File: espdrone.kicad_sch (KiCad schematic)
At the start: 60 parts, among them J6 Conn_01x06, U2 USBLC6-2P6, U3 W25Q128JVP, Y1 Crystal_GND24

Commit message: Route some peripherals
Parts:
- removed C6: 100n, Capacitor_SMD:C_0402_1005Metric, symbol Device:C
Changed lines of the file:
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@@
 	)
 	(junction
-		(at 55.88 223.52)
-		(diameter 0)
-		(color 0 0 0 0)
-	)
-	(junction
 		(at 109.22 264.16)
 		(diameter 0)
@@
 	)
 	(junction
-		(at 44.45 233.68)
-		(diameter 0)
-		(color 0 0 0 0)
-	)
-	(junction
 		(at 232.41 220.98)
 		(diameter 0)
@@
 	(wire
 		(pts
-			(xy 44.45 232.41) (xy 44.45 233.68)
+			(xy 44.45 232.41) (xy 44.45 234.95)
 		)
 		(stroke
@@
 	(wire
 		(pts
-			(xy 55.88 233.68) (xy 44.45 233.68)
-		)
-		(stroke
-			(width 0)
-			(type default)
-		)
-	)
-	(wire
-		(pts
 			(xy 255.27 231.14) (xy 255.27 232.41)
 		)
@@
 	(wire
 		(pts
-			(xy 55.88 232.41) (xy 55.88 233.68)
-		)
-		(stroke
-			(width 0)
-			(type default)
-		)
-	)
-	(wire
-		(pts
 			(xy 285.75 142.24) (xy 285.75 151.13)
 		)
@@
 	(wire
 		(pts
-			(xy 44.45 233.68) (xy 44.45 234.95)
-		)
-		(stroke
-			(width 0)
-			(type default)
-		)
-	)
-	(wire
-		(pts
 			(xy 217.17 166.37) (xy 218.44 166.37)
 		)
@@
 	(wire
 		(pts
-			(xy 55.88 223.52) (xy 55.88 224.79)
-		)
-		(stroke
-			(width 0)
-			(type default)
-		)
-	)
-	(wire
-		(pts
-			(xy 55.88 223.52) (xy 44.45 223.52)
-		)
-		(stroke
-			(width 0)
-			(type default)
-		)
-	)
-	(wire
-		(pts
 			(xy 87.63 73.66) (xy 87.63 74.93)
 		)
@@
 	(wire
 		(pts
-			(xy 55.88 223.52) (xy 106.68 223.52)
+			(xy 44.45 223.52) (xy 106.68 223.52)
 		)
 		(stroke
@@
 					(unit 1)
 				)
-			)
-		)
-	)
-	(symbol
-		(lib_id "Device:C")
-		(at 55.88 228.6 0)
-		(mirror y)
-		(unit 1)
-		(body_style 1)
-		(exclude_from_sim no)
-		(in_bom yes)
-		(on_board yes)
-		(in_pos_files yes)
-		(dnp no)
-		(property "Reference" "C6"
-			(at 52.832 227.33 0)
-			(show_name no)
-			(do_not_autoplace no)
-			(effects
-				(font
-					(size 1.27 1.27)
-				)
-				(justify left)
-			)
-		)
-		(property "Value" "100n"
-			(at 53.086 229.87 0)
-			(show_name no)
-			(do_not_autoplace no)
-			(effects
-				(font
-					(size 1.27 1.27)
-				)
-				(justify left)
-			)
-		)
-		(property "Footprint" "Capacitor_SMD:C_0402_1005Metric"
-			(at 54.9148 232.41 0)
-			(hide yes)
-			(show_name no)
-			(do_not_autoplace no)
-			(effects
-				(font
-					(size 1.27 1.27)
-				)
-			)
-		)
-		(property "Datasheet" ""
-			(at 55.88 228.6 0)
-			(hide yes)
-			(show_name no)
-			(do_not_autoplace no)
-			(effects
-				(font
-					(size 1.27 1.27)
-				)
-			)
-		)
-		(property "Description" "Unpolarized capacitor"
-			(at 55.88 228.6 0)
-			(hide yes)
-			(show_name no)
-			(do_not_autoplace no)
-			(effects
-				(font
-					(size 1.27 1.27)
-				)
-			)
-		)
-		(pin "1"
-		)
-		(pin "2"
-		)
-		(instances
-			(project "espdrone"
-				(path "/6e047eb1-70b3-49d8-916c-92a2df32e839"
-					(reference "C6")
-					(unit 1)
-				)

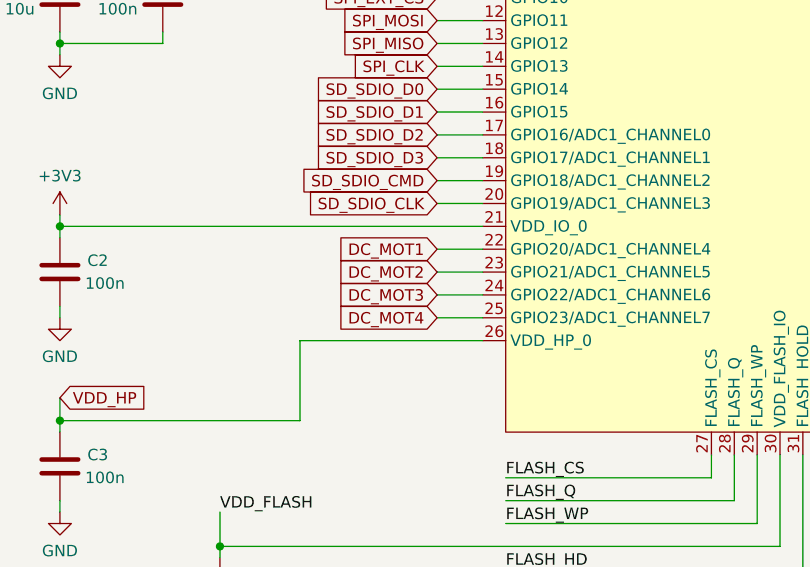
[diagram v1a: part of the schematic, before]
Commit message: Remove brushed motor control and WS2812B LEDs
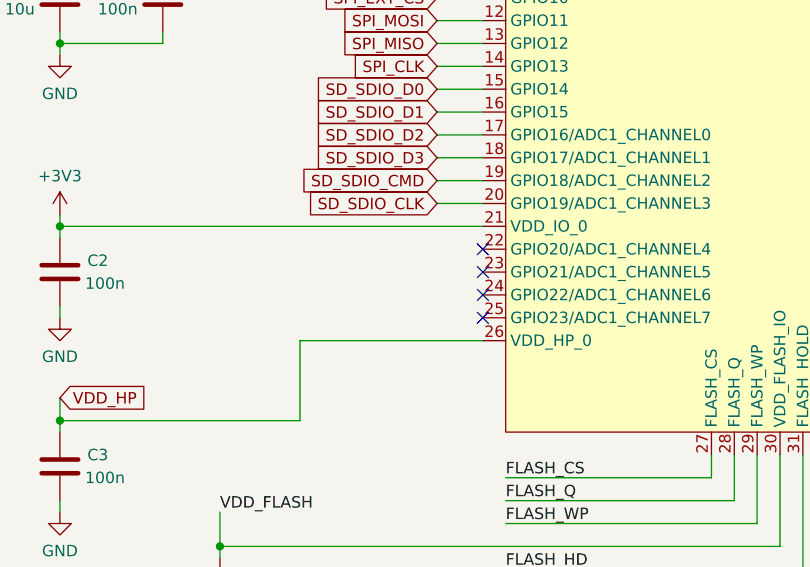
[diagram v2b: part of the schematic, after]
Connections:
- net DC_MOT1: no longer names the net of U1.22 (GPIO20/ADC1_CHANNEL4)
- net DC_MOT2: no longer names the net of U1.23 (GPIO21/ADC1_CHANNEL5)
- net DC_MOT3: no longer names the net of U1.24 (GPIO22/ADC1_CHANNEL6)
- net DC_MOT4: no longer names the net of U1.25 (GPIO23/ADC1_CHANNEL7)
- no-connect marks 27 -> 31
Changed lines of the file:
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@@
 	)
 	(no_connect
+		(at 73.66 190.5)
+	)
+	(no_connect
 		(at 157.48 213.36)
 	)
@@
 	)
 	(no_connect
+		(at 73.66 198.12)
+	)
+	(no_connect
 		(at 190.5 173.99)
 	)
@@
 	)
 	(no_connect
+		(at 73.66 195.58)
+	)
+	(no_connect
 		(at 132.08 213.36)
 	)
@@
 		(at 73.66 142.24)
 	)
+	(no_connect
+		(at 73.66 193.04)
+	)
 	(wire
 		(pts
@@
 	(wire
 		(pts
-			(xy 68.58 195.58) (xy 73.66 195.58)
-		)
-		(stroke
-			(width 0)
-			(type default)
-		)
-	)
-	(wire
-		(pts
 			(xy 147.32 233.68) (xy 177.8 233.68)
 		)
@@
 	(wire
 		(pts
-			(xy 68.58 198.12) (xy 73.66 198.12)
-		)
-		(stroke
-			(width 0)
-			(type default)
-		)
-	)
-	(wire
-		(pts
 			(xy 157.48 116.84) (xy 165.1 116.84)
 		)
@@
 	(wire
 		(pts
-			(xy 68.58 193.04) (xy 73.66 193.04)
-		)
-		(stroke
-			(width 0)
-			(type default)
-		)
-	)
-	(wire
-		(pts
 			(xy 287.02 46.99) (xy 287.02 41.91)
 		)
@@
 	(wire
 		(pts
-			(xy 68.58 190.5) (xy 73.66 190.5)
-		)
-		(stroke
-			(width 0)
-			(type default)
-		)
-	)
-	(wire
-		(pts
 			(xy 44.45 223.52) (xy 106.68 223.52)
 		)
@@
 		)
 	)
-	(global_label "DC_MOT3"
-		(shape input)
-		(at 68.58 195.58 180)
-		(fields_autoplaced yes)
-		(effects
-			(font
-				(size 1.27 1.27)
-			)
-			(justify right)
-		)
-		(property "Intersheetrefs" "${INTERSHEET_REFS}"
-			(at 57.1282 195.58 0)
-			(hide yes)
-			(show_name no)
-			(do_not_autoplace no)
-			(effects
-				(font
-					(size 1.27 1.27)
-				)
-				(justify right)
-			)
-		)
-	)
 	(global_label "DSHOT_2"
 		(shape input)
@@
 		)
 	)
-	(global_label "DC_MOT4"
-		(shape input)
-		(at 68.58 198.12 180)
-		(fields_autoplaced yes)
-		(effects
-			(font
-				(size 1.27 1.27)
-			)
-			(justify right)
-		)
-		(property "Intersheetrefs" "${INTERSHEET_REFS}"
-			(at 57.1282 198.12 0)
-			(hide yes)
-			(show_name no)
-			(do_not_autoplace no)
-			(effects
-				(font
-					(size 1.27 1.27)
-				)
-				(justify right)
-			)
-		)
-	)
-	(global_label "DC_MOT2"
-		(shape input)
-		(at 68.58 193.04 180)
-		(fields_autoplaced yes)
-		(effects
-			(font
-				(size 1.27 1.27)
-			)
-			(justify right)
-		)
-		(property "Intersheetrefs" "${INTERSHEET_REFS}"
-			(at 57.1282 193.04 0)
-			(hide yes)
-			(show_name no)
-			(do_not_autoplace no)
-			(effects
-				(font
-					(size 1.27 1.27)
-				)
-				(justify right)
-			)
-		)
-	)
 	(global_label "TELEMETRY"
 		(shape input)
@@
 			)
 		)
-	)
-	(global_label "DC_MOT1"
-		(shape input)
-		(at 68.58 190.5 180)
-		(fields_autoplaced yes)
-		(effects
-			(font
-				(size 1.27 1.27)
-			)
-			(justify right)
-		)
-		(property "Intersheetrefs" "${INTERSHEET_REFS}"
-			(at 57.1282 190.5 0)
-			(hide yes)
-			(show_name no)
-			(do_not_autoplace no)
-			(effects
-				(font
-					(size 1.27 1.27)
-				)
-				(justify right)
-			)
-		)

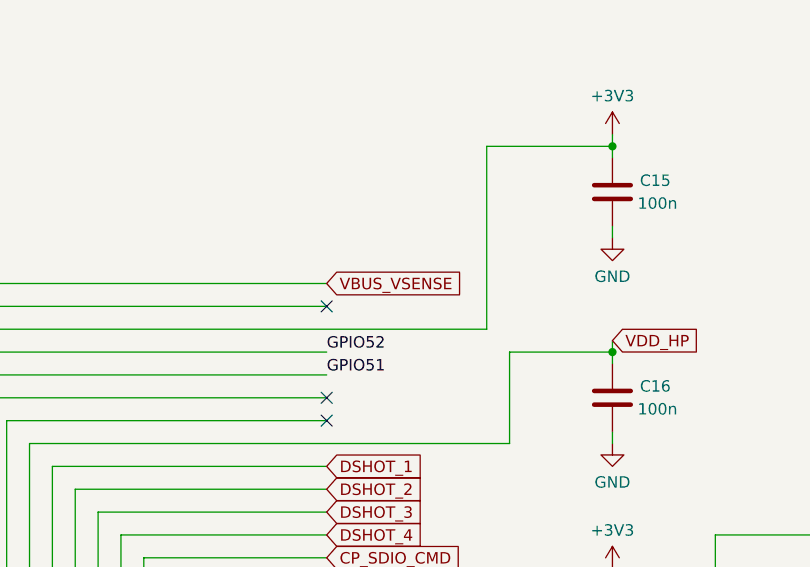
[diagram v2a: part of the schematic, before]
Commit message: Remove external SPI connections and switch voltage measurement from VBUS to +BAT
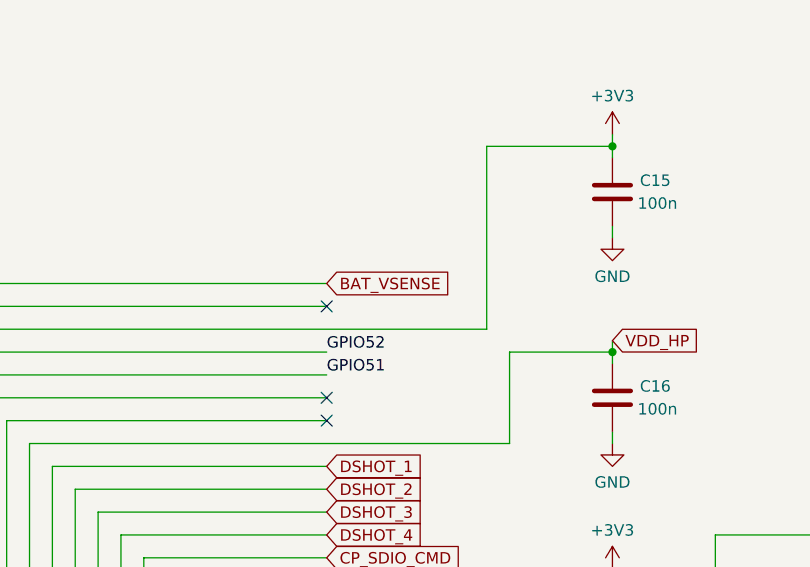
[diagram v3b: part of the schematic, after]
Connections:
- net VBUS_VSENSE renamed BAT_VSENSE
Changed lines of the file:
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@@
 		)
 	)
-	(global_label "VBUS_VSENSE"
+	(global_label "BAT_VSENSE"
 		(shape input)
 		(at 165.1 73.66 0)
@@
 		)
 		(property "Intersheetrefs" "${INTERSHEET_REFS}"
-			(at 181.0875 73.66 0)
+			(at 179.5151 73.66 0)
 			(hide yes)
 			(show_name no)

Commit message: New board cuedge cut
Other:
- company: All-in-one drone flight controller, camera and ESC -> All-in-one drone flight controller, camera and 2S-3S ESC
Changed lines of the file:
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@@
 		(date "2026-08-28")
 		(rev "1.0")
-		(company "All-in-one drone flight controller, camera and ESC")
+		(company "All-in-one drone flight controller, camera and 2S-3S ESC")
 		(comment 1 "ESP32 P4 + ESP32 C5, 4xAM32 ESCs")
-		(comment 2 "1S DC motors, 2S-3S BLDC motors")
 	)
 	(rectangle

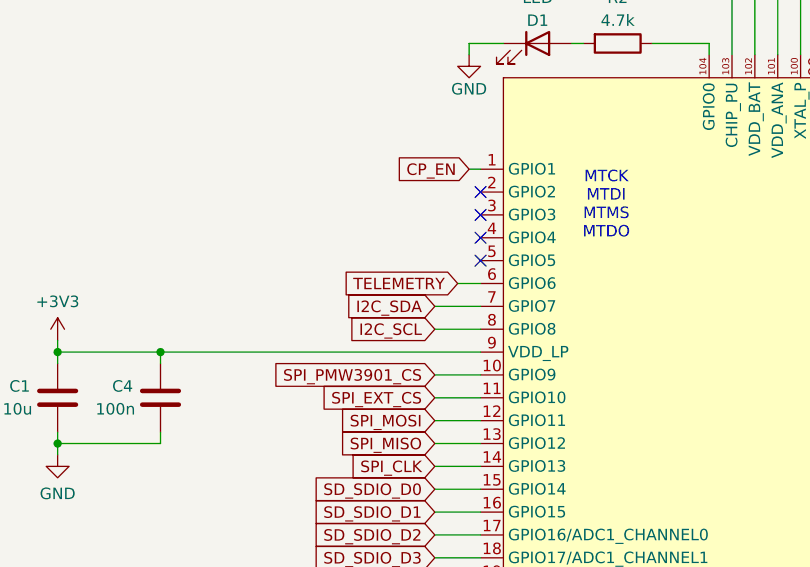
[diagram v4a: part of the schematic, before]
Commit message: Small routing changes
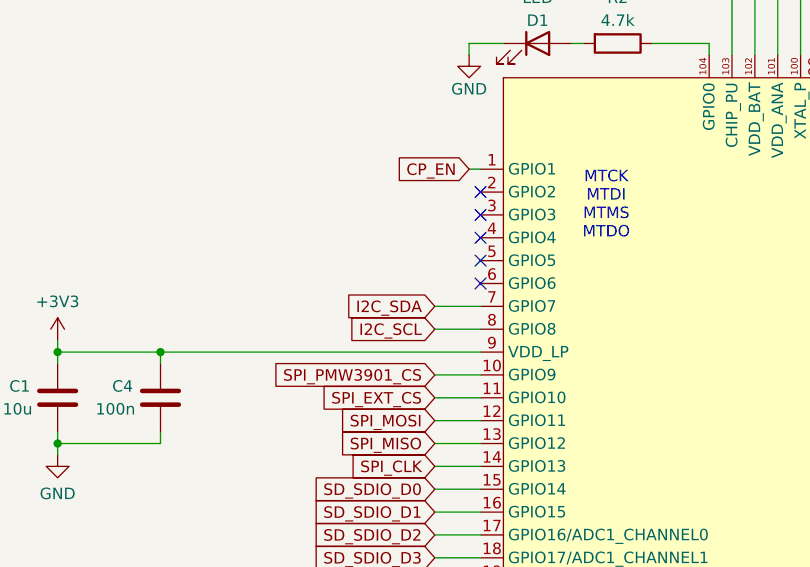
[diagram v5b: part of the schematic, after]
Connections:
- net TELEMETRY: no longer names the net of U1.6 (GPIO6)
- no-connect marks 31 -> 32
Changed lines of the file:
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@@
 	)
 	(no_connect
+		(at 73.66 149.86)
+	)
+	(no_connect
 		(at 190.5 168.91)
 	)
@@
 	(wire
 		(pts
-			(xy 71.12 149.86) (xy 73.66 149.86)
-		)
-		(stroke
-			(width 0)
-			(type default)
-		)
-	)
-	(wire
-		(pts
 			(xy 372.11 71.12) (xy 372.11 72.39)
 		)
@@
 			)
 		)
-	)
-	(global_label "TELEMETRY"
-		(shape input)
-		(at 71.12 149.86 180)
-		(fields_autoplaced yes)
-		(effects
-			(font
-				(size 1.27 1.27)
-			)
-			(justify right)
-		)
-		(property "Intersheetrefs" "${INTERSHEET_REFS}"
-			(at 57.9145 149.86 0)
-			(hide yes)
-			(show_name no)
-			(do_not_autoplace no)
-			(effects
-				(font
-					(size 1.27 1.27)
-				)
-				(justify right)
-			)
-		)

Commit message: Minimize passive footprints again and switch ESC mcu to smaller footprint
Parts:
- removed J6: Conn_01x06, easyeda2kicad:Connector_Pad_1.27mm_1x06, symbol Connector_Generic:Conn_01x06
- removed R8, R9: 10, Resistor_SMD:R_0402_1005Metric, symbol Device:R
- added R49, R51: 10k, Capacitor_SMD:C_0201_0603Metric, symbol Device:R
- C10, C13, C14, C15, C16, C17, C19, C2, C20, C21, C22, C23, C24, C26, C28, C3, C34, C4, C9: footprint Capacitor_SMD:C_0402_1005Metric -> Capacitor_SMD:C_0201_0603Metric
- C29: footprint Capacitor_SMD:C_0603_1608Metric -> Capacitor_SMD:C_0402_1005Metric
- C7: value 100n -> 1u
- R1, R10, R11, R12, R15, R161, R162, R163, R164, R24, R5: footprint Resistor_SMD:R_0402_1005Metric -> Resistor_SMD:R_0201_0603Metric
- R6, R7: footprint Resistor_SMD:R_0402_1005Metric -> Capacitor_SMD:C_0201_0603Metric
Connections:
- net SPI_EXT_CS is gone; now on net SPI_PMW3901_CS: U1.11 (GPIO10)
- net +3V3: now also R49.2, R51.2
- net I2C_SCL: now also R49.1
- net I2C_SDA: now also R51.1
- net SPI_PMW3901_CS: no longer U1.10 (GPIO9)
- net SD_SDIO_CLK: no longer names the net of U1.20 (GPIO19/ADC1_CHANNEL3)
- net SD_SDIO_CMD: no longer names the net of U1.19 (GPIO18/ADC1_CHANNEL2)
- net SD_SDIO_D0: no longer names the net of U1.15 (GPIO14)
- net SD_SDIO_D1: no longer names the net of U1.16 (GPIO15)
- net SD_SDIO_D2: no longer names the net of U1.17 (GPIO16/ADC1_CHANNEL0)
- net SD_SDIO_D3: no longer names the net of U1.18 (GPIO17/ADC1_CHANNEL1)
- no-connect marks 32 -> 39
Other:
- note removed: "UART+GPIO breakout"
- moved on the sheet: C5

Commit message: Apply ESC layout to all 4 ESCs
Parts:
- USB1: footprint easyeda2kicad:USB-C-SMD_TYPE-C-16PIN-2MD-073 -> easyeda2kicad:USB-C-SMD_TYPE-C-16P-USB4110-GF-A
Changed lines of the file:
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@@
 			)
 		)
-		(property "Footprint" "easyeda2kicad:USB-C-SMD_TYPE-C-16PIN-2MD-073"
+		(property "Footprint" "easyeda2kicad:USB-C-SMD_TYPE-C-16P-USB4110-GF-A"
 			(at 275.59 82.55 0)
 			(hide yes)

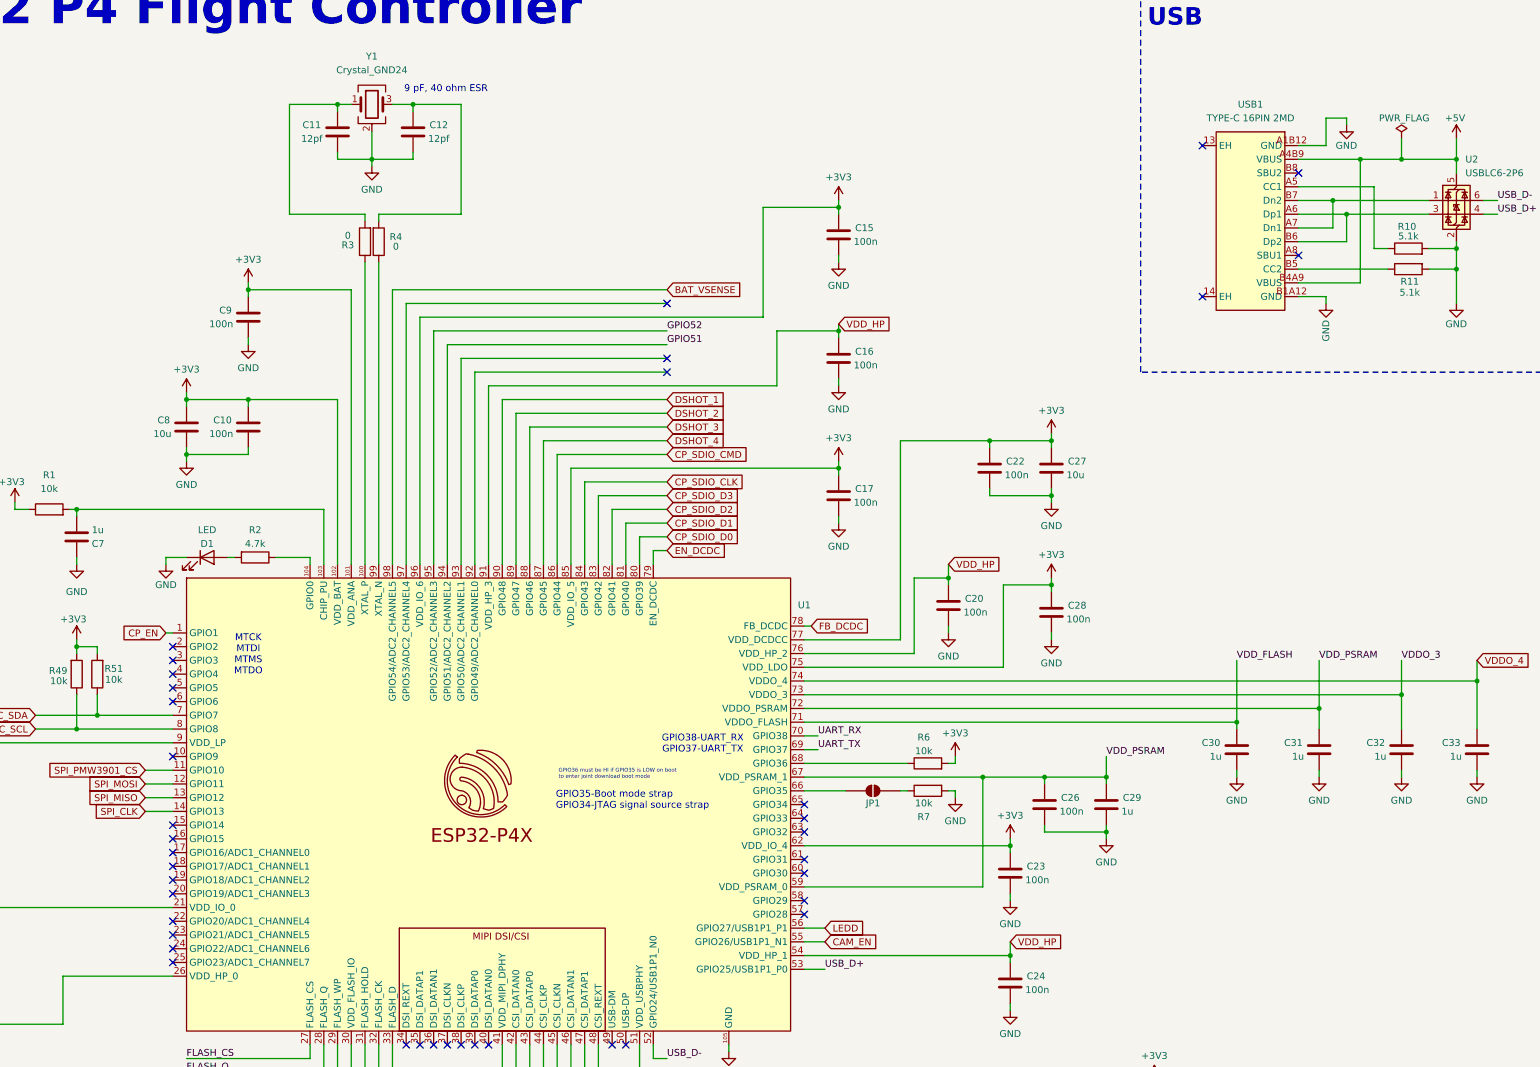
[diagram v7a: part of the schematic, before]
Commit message: Start laying out FC section
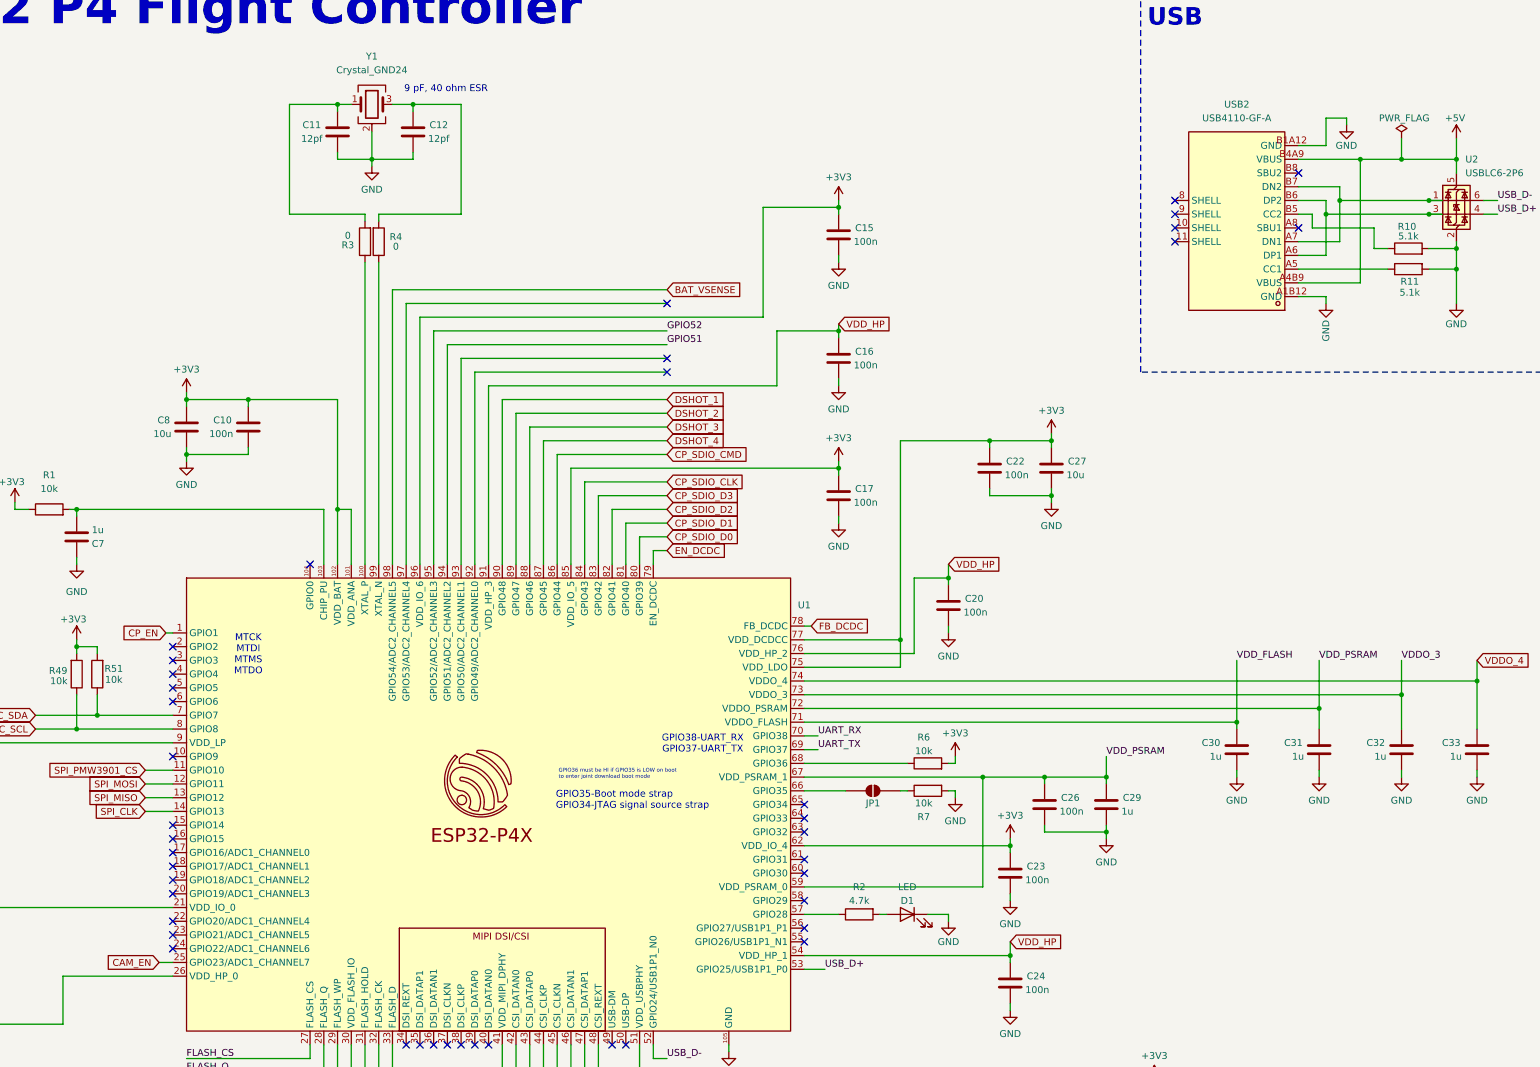
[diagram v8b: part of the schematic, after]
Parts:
- removed C28, C9: 100n, Capacitor_SMD:C_0201_0603Metric, symbol Device:C
- removed USB1: TYPE-C 16PIN 2MD, easyeda2kicad:USB-C-SMD_TYPE-C-16P-USB4110-GF-A, symbol easyeda2kicad:TYPE-C16PIN2MD
- added USB2: USB4110-GF-A, easyeda2kicad:USB-C-SMD_TYPE-C-16P-USB4110-GF-A, symbol easyeda2kicad:USB4110-GF-A
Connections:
- net +5V: now also USB2.A4B9 (VBUS), USB2.B4A9 (VBUS)
- net CAM_EN: now also U1.25 (GPIO23/ADC1_CHANNEL7); no longer U1.55 (GPIO26/USB1P1_N1)
- net GND: now also USB2.A1B12 (GND), USB2.B1A12 (GND)
- net at R10.1: now also USB2.B5 (CC2)
- net at U1.104 (GPIO0): no longer R2.1
- net at U2.3 (I/O2): now also USB2.A6 (DP1), USB2.B6 (DP2)
- net at U2.1 (I/O1): now also USB2.A7 (DN1), USB2.B7 (DN2)
- net at R11.1: now also USB2.A5 (CC1)
- net at U1.57 (GPIO28): now also R2.1
- net LEDD: no longer names the net of U1.56 (GPIO27/USB1P1_P1)
- no-connect marks 39 -> 42
